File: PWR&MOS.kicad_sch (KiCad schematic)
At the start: 27 parts, among them Q1 IRLZ44N, Q2 IRLZ44N, Q3 IRLZ44N, Q4 IRLZ44N, Q5 IRLZ44N, Q6 IRLZ44N

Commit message: updated layout, power supply schematic
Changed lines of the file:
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@@
+	)
+	(junction
+		(at 100.33 138.43)
+		(diameter 0)
+		(color 0 0 0 0)
 	)
 	(junction
@@
 		(color 0 0 0 0)
 	)
-	(junction
-		(at 100.33 138.43)
-		(diameter 0)
-		(color 0 0 0 0)
-	)
 	(wire
 		(pts
@@
 	(wire
 		(pts
-			(xy 100.33 138.43) (xy 100.33 140.97)
+			(xy 100.33 138.43) (xy 100.33 151.13)
 		)
 		(stroke
@@
 	(symbol
 		(lib_id "power:-BATT")
-		(at 100.33 140.97 180)
+		(at 100.33 151.13 180)
 		(unit 1)
 		(body_style 1)
@@
 		(fields_autoplaced yes)
 		(property "Reference" "#PWR06"
-			(at 100.33 137.16 0)
+			(at 100.33 147.32 0)
 			(hide yes)
 			(show_name no)
@@
 		)
 		(property "Value" "-BATT"
-			(at 100.33 146.05 0)
+			(at 100.33 156.21 0)
 			(show_name no)
 			(do_not_autoplace no)
@@
 		)
 		(property "Footprint" ""
-			(at 100.33 140.97 0)
+			(at 100.33 151.13 0)
 			(hide yes)
 			(show_name no)
@@
 		)
 		(property "Datasheet" ""
-			(at 100.33 140.97 0)
+			(at 100.33 151.13 0)
 			(hide yes)
 			(show_name no)
@@
 		)
 		(property "Description" "Power symbol creates a global label with name \"-BATT\""
-			(at 100.33 140.97 0)
-			(hide yes)
-			(show_name no)
+			(at 100.33 151.13 0)
+			(hide yes)
+			(show_name no)

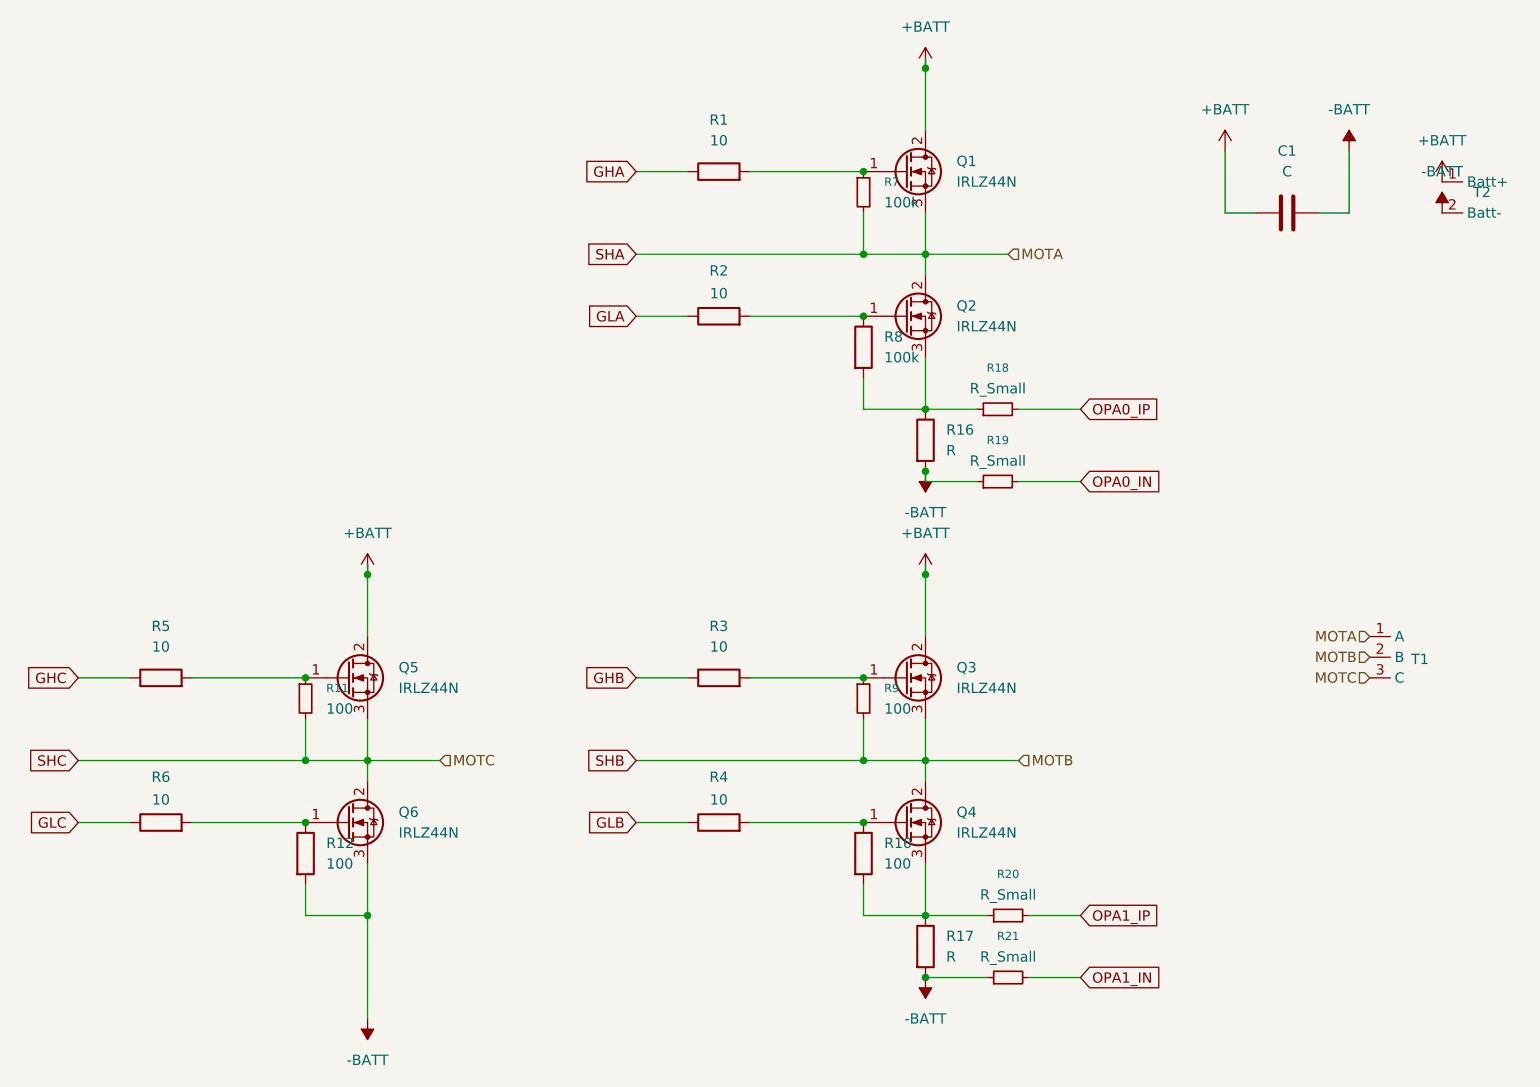
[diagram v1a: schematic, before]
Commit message: Fix ESC power, gate drive and current sensing schematics
Correct the buck converter and MCU symbols, bootstrap networks, MOSFET pulldowns and current sensing components. Migrate project libraries, synchronize PCB footprints and ground nets, and resolve ERC errors and warnings. Include LCSC BOMs and design notes; PCB routing remains incomplete.
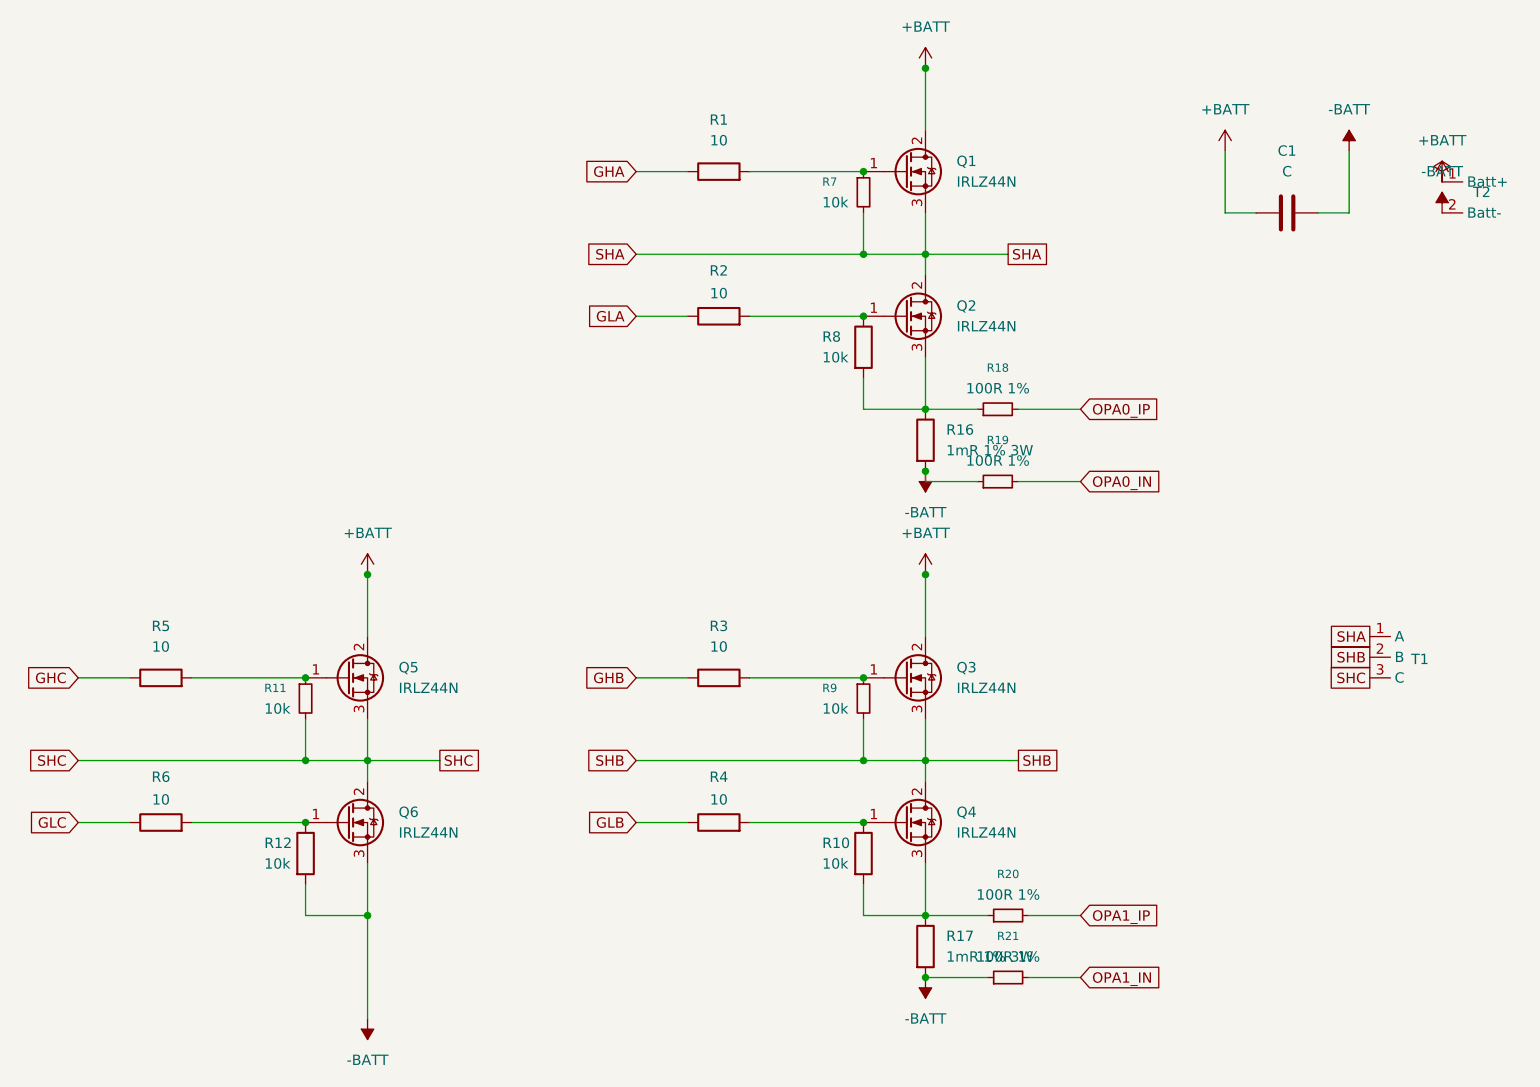
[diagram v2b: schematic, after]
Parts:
- C1: footprint Vesc_footprints:Capacitor_50v_1000uf -> Custom_footprints:C_Radial_P5mm_AsRouted
- R10, R11, R12, R9: value 100 -> 10k; LCSC (none) -> C25744; MPN (none) -> 0402WGF1002TCE; Manufacturer (none) -> UNI-ROYAL; Power (none) -> 62.5mW; Tolerance (none) -> 1%
- R16, R17: value R -> 1mR 1% 3W; footprint Resistor_SMD:R_2010_5025Metric_Pad1.40x2.65mm_HandSolder -> Resistor_SMD:R_2512_6332Metric; LCSC (none) -> C2903470; MPN (none) -> HoJLR2512-3W-1mR-1%; Manufacturer (none) -> Milliohm
- R18, R19, R20, R21: value R_Small -> 100R 1%; LCSC (none) -> C22775; MPN (none) -> 0603WAF1000T5E; Manufacturer (none) -> UNI-ROYAL
- R7, R8: value 100k -> 10k; LCSC (none) -> C25744; MPN (none) -> 0402WGF1002TCE; Manufacturer (none) -> UNI-ROYAL; Power (none) -> 62.5mW; Tolerance (none) -> 1%
- T1: footprint Vesc_footprints:ABC_Terminal -> Custom_footprints:ABC_Terminal; symbol VESC_Custom:ABC_terminal -> Custom:ABC_terminal
- T2: footprint Vesc_footprints:Untitled -> Custom_footprints:Battery_Wire_Pads_P10mm; symbol VESC_Custom:Power_Terminal -> Custom:Power_Terminal
